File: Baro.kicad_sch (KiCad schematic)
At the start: 4 parts, among them U5 LPS22HB, U7 MS5607-02BA

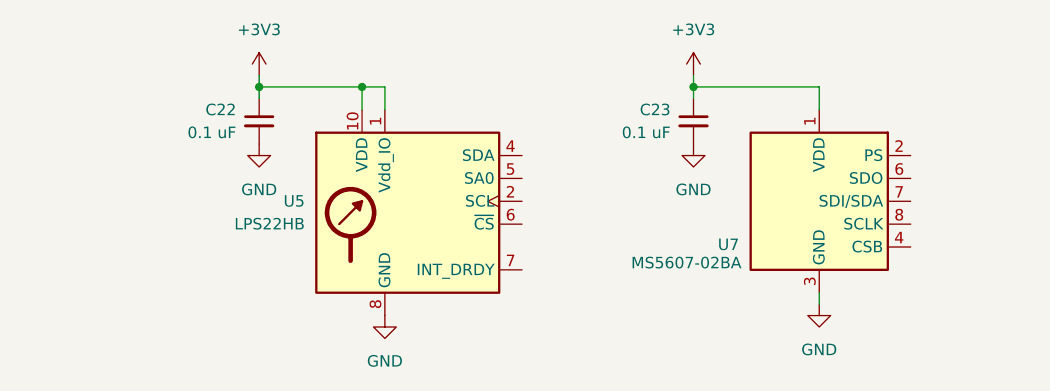
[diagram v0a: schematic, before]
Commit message: Wired barometers and GPS up, added misc LEDs, tidy-up
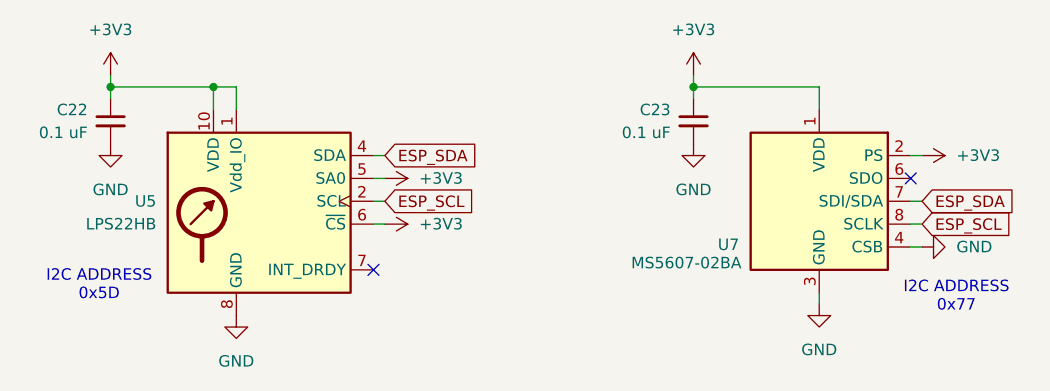
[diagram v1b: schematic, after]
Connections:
- net +3V3: now also U5.5 (SA0), U5.6 (~{CS}), U7.2 (PS)
- net GND: now also U7.4 (CSB), U7.5 (CSB)
- net ESP_SCL: now reaches U5.2 (SCL)
- net ESP_SCL: now also U7.8 (SCLK)
- net ESP_SDA: now reaches U5.4 (SDA)
- net ESP_SDA: now also U7.7 (SDI/SDA)
- no-connect marks 0 -> 2
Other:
- note added: "I2C ADDRESS 0x5D"
- note added: "I2C ADDRESS 0x77"
- moved on the sheet: C22, U5

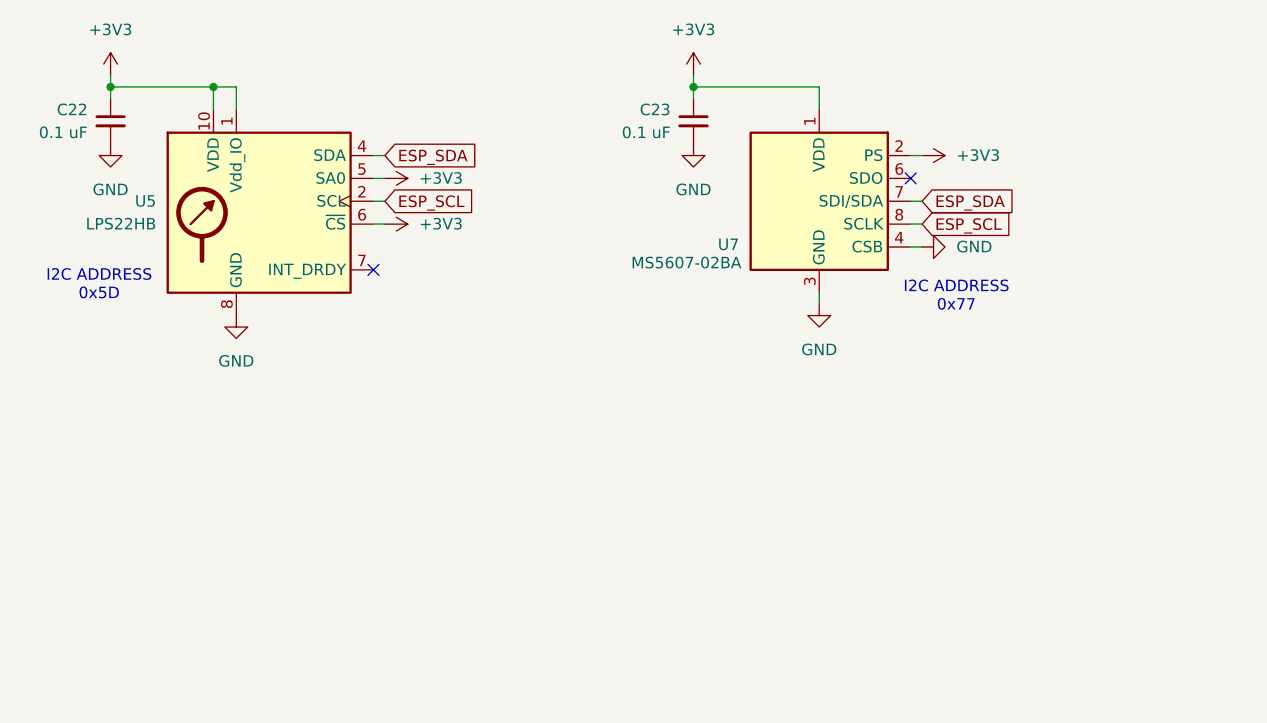
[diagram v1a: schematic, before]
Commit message: preliminary schematic wired, all footprints assigned, all laid out in PCB editor.
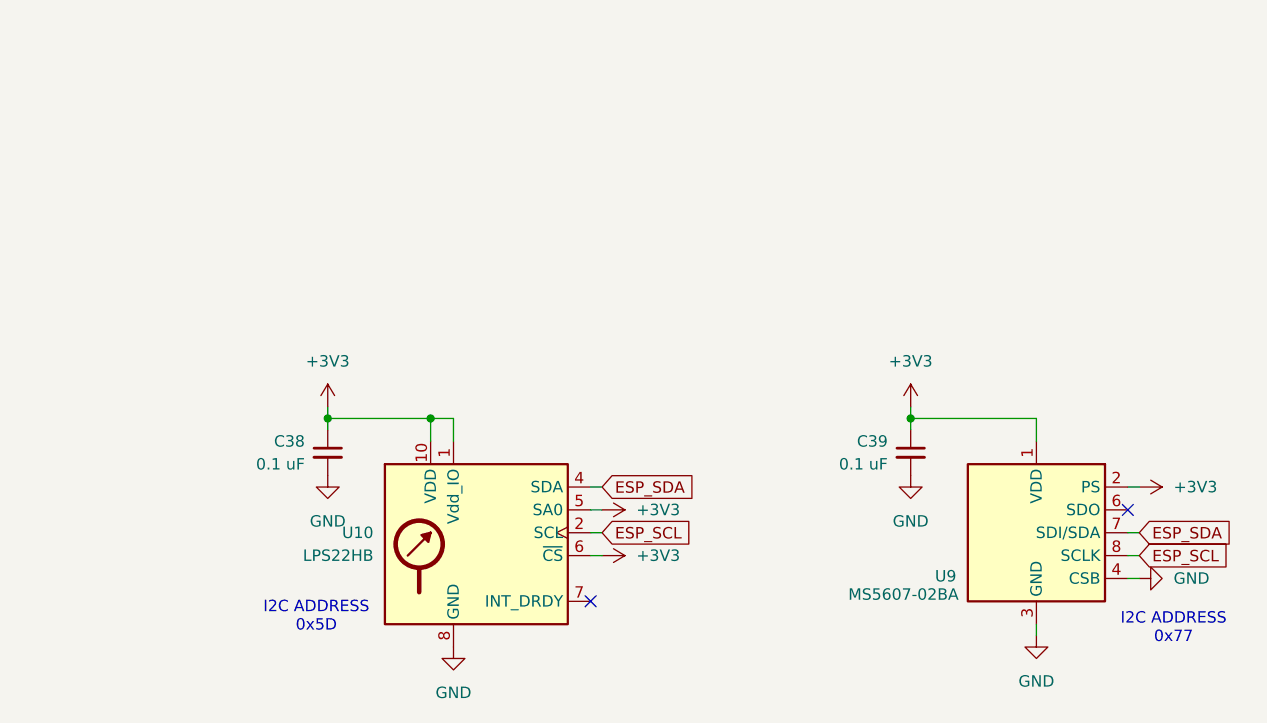
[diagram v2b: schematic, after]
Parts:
- renumbered C22 to C38, C23 to C39, U5 to U10, U7 to U9
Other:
- moved on the sheet: C38, C39, U10, U9

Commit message: reassigned some footprints, preliminary PCB layout
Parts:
- C38, C39: footprint Capacitor_SMD:C_0805_2012Metric -> Capacitor_SMD:C_0603_1608Metric
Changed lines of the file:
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@@
 			)
 		)
-		(property "Footprint" "Capacitor_SMD:C_0805_2012Metric"
+		(property "Footprint" "Capacitor_SMD:C_0603_1608Metric"
 			(at 163.83 83.82 0)
 			(effects
@@
 			)
 		)
-		(property "Footprint" "Capacitor_SMD:C_0805_2012Metric"
+		(property "Footprint" "Capacitor_SMD:C_0603_1608Metric"
 			(at 99.06 83.82 0)
 			(effects
